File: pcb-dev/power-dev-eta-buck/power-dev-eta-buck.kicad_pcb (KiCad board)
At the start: 2 copper layers, 21 x 11 mm, 26 parts, among them J1 Pin headers, J2 Pin headers, U1 ETA8121, U2 ETA3485

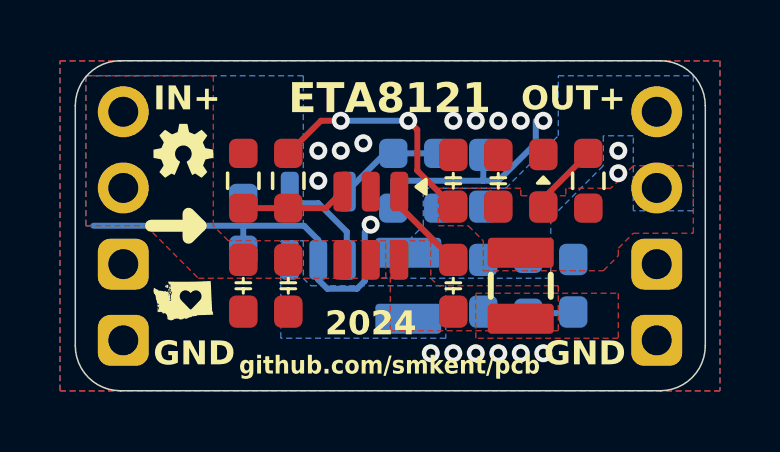
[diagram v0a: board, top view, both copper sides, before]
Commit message: Add additional GND path on back side
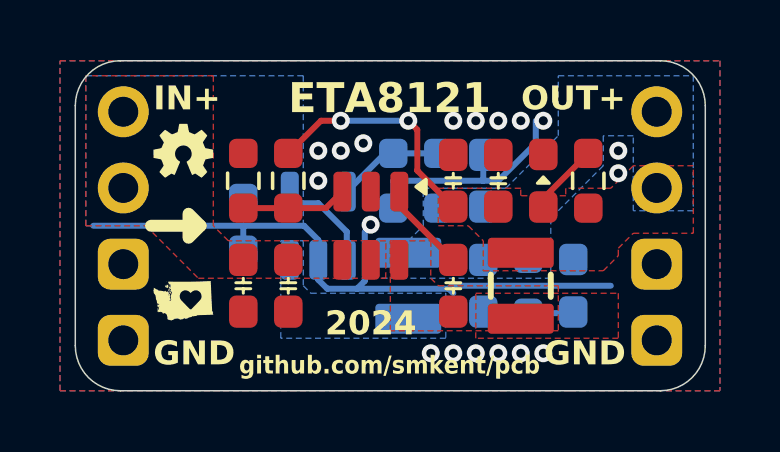
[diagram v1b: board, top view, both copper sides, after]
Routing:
- net GND: track 21.1 -> 29.8 mm
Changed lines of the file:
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@@
+	)
+	(segment
+		(start 115.85 72.1)
+		(end 116 72.25)
+		(width 0.2)
+		(layer "B.Cu")
+		(net 1)
 	)
 	(segment
@@
 	(segment
 		(start 112.790552 72.1)
+		(end 115.85 72.1)
+		(width 0.2)
+		(layer "B.Cu")
+		(net 1)
+	)
+	(segment
+		(start 115.95 72)
+		(end 121.25 72)
+		(width 0.2)
+		(layer "B.Cu")
+		(net 1)
+	)
+	(segment
+		(start 112.790552 72.1)
 		(end 113.05 71.840552)
+		(width 0.2)
+		(layer "B.Cu")
+		(net 1)
+	)
+	(segment
+		(start 115.85 72.1)
+		(end 115.95 72)
 		(width 0.2)
 		(layer "B.Cu")
@@
 		(polygon
 			(pts
-				(xy 111 71.75) (xy 111.25 72) (xy 115.75 72) (xy 115.75 73.75) (xy 110.25 73.75) (xy 110.25 70.5)
+				(xy 111 72) (xy 111.25 72.25) (xy 115.75 72.25) (xy 115.75 73.75) (xy 110.25 73.75) (xy 110.25 70.5)
 				(xy 111 70.5)
 			)
